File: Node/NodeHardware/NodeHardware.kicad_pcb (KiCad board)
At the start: 4 copper layers, 80 x 106 mm, 241 parts, among them J1 CONN_I2C, J10 DIG_IO_03, J11 ANA_IN_02, J12 PWR_OUT, J13 DIG_IO_02, J14 DIG_IO_04, J15 ANA_IN_03, J16 DIG_OUT_02, J17 ANA_IN_04, J2 USB_C_Receptacle_16P, J3 CONN_SPI, J4 PWR_IN, J5 ESP32_JTAG, J6 BATT, J7 ANA_IN_01, J8 DIG_OUT_01, J9 DIG_IO_01, Q1 AO3401A, Q2 AO3401A, Q3 2N7002, Q4 2N7002, Q5 AO3400A, Q6 AO3400A, SW1 RST, SW2 BOOT, SW3 BTN, U1 TPS565201DDCR, U2 CH340C, U3 SIM7000G_DEVBoard, U4 SPX3819M5-L-3-3, U5 MCP73831-2-OT, U6 ESP32-S3-WROOM-1, U7 ADS1220xPW, U8 ADS1220xPW

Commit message: Finish v1 of PCB layout
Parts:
- removed the C33 at (226.3, 111.4)
- removed the C33 at (243.3, 93.5)
- removed C37: 100n, Capacitor_SMD:C_0805_2012Metric
- removed the D15 at (263.9, 98.1)
- removed the D16 at (263.9, 102.3)
- removed the D23 at (256.8, 75.1)
- removed D27: BAT54S, Package_TO_SOT_SMD:SOT-23
- removed the R65 at (201.8, 93.4)
- removed the R65 at (206.2, 111.1)
- removed the R69 at (261.9, 71.6)
- removed the R69 at (206.2, 105.2)
- removed the R77 at (206.2, 114.0)
- removed the TP10 at (297.2, 141.0)
- removed the TP21 at (214.3, 78.5)
- removed the TP30 at (214.3, 72.4)
- removed the TP31 at (211.3, 75.5)
- removed TP37, TP53: TP_DIG_IO_06, TestPoint:TestPoint_Pad_D1.0mm
- removed TP38: TP_SPI_MISO, TestPoint:TestPoint_Pad_D1.0mm
- removed TP39: TP_SPI_CS_EXT, TestPoint:TestPoint_Pad_D1.0mm
- removed TP40: TP_DIG_OUT_01, TestPoint:TestPoint_Pad_D1.0mm
- removed TP41: TP_DIG_OUT_02, TestPoint:TestPoint_Pad_D1.0mm
- removed TP42: TP_ANA_IN_01, TestPoint:TestPoint_Pad_D1.0mm
- removed TP43: TP_ANA_IN_02, TestPoint:TestPoint_Pad_D1.0mm
- removed TP44: TP_ANA_IN_01_UC, TestPoint:TestPoint_Pad_D1.0mm
- removed TP45: TP_ANA_IN_02_UC, TestPoint:TestPoint_Pad_D1.0mm
- removed TP46: TP_ANA_IN_04, TestPoint:TestPoint_Pad_D1.0mm
- removed TP47: TP_ANA_IN_03, TestPoint:TestPoint_Pad_D1.0mm
- removed TP48: TP_DIG_IO_01, TestPoint:TestPoint_Pad_D1.0mm
- removed TP49: TP_DIG_IO_03, TestPoint:TestPoint_Pad_D1.0mm
- removed TP49: TP_DIG_IO_02, TestPoint:TestPoint_Pad_D1.0mm
- removed TP50: TP_ANA_IN_04_UC, TestPoint:TestPoint_Pad_D1.0mm
- removed TP51: TP_ANA_IN_03_UC, TestPoint:TestPoint_Pad_D1.0mm
- removed TP52: TP_DIG_IO_04, TestPoint:TestPoint_Pad_D1.0mm
- removed TP53: TP_DIG_IO_05, TestPoint:TestPoint_Pad_D1.0mm
- removed the TP6 at (248.6, 148.0)
- added C33: 100n, Capacitor_SMD:C_0805_2012Metric, F.Cu at (172.4, 124.4)
- added D21: BLUE, LED_SMD:LED_1210_3225Metric, F.Cu at (170.4, 105.2)
- added D24: BAT54S, Package_TO_SOT_SMD:SOT-23, F.Cu at (170.5, 71.1)
- added D26: BLUE, LED_SMD:LED_1210_3225Metric, F.Cu at (170.4, 74.7)
- added H1: GSM_MountingHole, MountingHole:MountingHole_3.2mm_M3_Pad_Via, F.Cu at (164.2, 100.6)
- added R65: 10k, Resistor_SMD:R_0805_2012Metric, F.Cu at (174.1, 101.5)
- added R69: 10k, Resistor_SMD:R_0805_2012Metric, F.Cu at (174.1, 105.2)
- added R73: 47R, Resistor_SMD:R_0805_2012Metric, F.Cu at (158.0, 113.4)
- added R78: 10k, Resistor_SMD:R_0805_2012Metric, F.Cu at (169.8, 68.0)
- added R79: 10k, Resistor_SMD:R_0805_2012Metric, F.Cu at (174.1, 84.7)
- added TP13: TP_I2C_SCL, TestPoint:TestPoint_Pad_D1.0mm, F.Cu at (123.4, 66.7)
- added TP24: TP_DIG_IO_02, TestPoint:TestPoint_Pad_D1.0mm, F.Cu at (167.4, 91.1)
- added TP33: TP_ANA_IN_01_UC, TestPoint:TestPoint_Pad_D1.0mm, F.Cu at (162.7, 118.2)
- added TP35: TP_ANA_IN_04_UC, TestPoint:TestPoint_Pad_D1.0mm, F.Cu at (162.7, 120.5)
- added TP9: TP_UART0_TX, TestPoint:TestPoint_Pad_D1.0mm, F.Cu at (160.8, 57.5)
- D17: value YELLOW -> BAT54S; footprint LED_SMD:LED_1210_3225Metric -> Package_TO_SOT_SMD:SOT-23
- D20: value BAT54S -> 3V6; footprint Package_TO_SOT_SMD:SOT-23 -> Diode_SMD:D_SOD-123
- D22, D25: value BAT54S -> BLUE; footprint Package_TO_SOT_SMD:SOT-23 -> LED_SMD:LED_1210_3225Metric
- R23: value 47k -> 2k
- R70: value 47R -> 10k
- R74: value 100R -> 47R
- R76: value 10k -> 100R
- TP11: value 3V3_Bypass_TP -> TP_SPI_CS_0; footprint TestPoint:TestPoint_Pad_D2.0mm -> TestPoint:TestPoint_Pad_D1.0mm
- TP12: value TP_UART0_TX -> TP_SPI_CS_1
- TP14: value TP_SPI_CS_0 -> TP_I2C_SDA
- TP15: value TP_SPI_CS_1 -> TP_DIGOUT_01
- TP16: value TP_I2C_SCL -> TP_DIGOUT_02
- TP17: value TP_I2C_SDA -> TP_GPIO6
- TP18: value TP_DIGOUT_01 -> TP_GPIO7
- TP19: value TP_DIGOUT_02 -> TP_GPIO8
- TP20: value TP_GPIO6 -> TP_GPIO9
- TP22: value TP_GPIO8 -> TP_GPIO11
- TP23: value TP_GPIO9 -> TP_DIG_IO_01
- TP25: value TP_GPIO11 -> TP_DIG_IO_03
- TP26: value TP_DIG_IO_01 -> TP_UART1_TX
- TP27: value TP_DIG_IO_02 -> TP_UART1_RX
- TP28: value TP_DIG_IO_03 -> TP_DIG_IO_04
- TP29: value TP_UART1_TX -> TP_DIG_IO_05
- TP32: value TP_DIG_IO_05 -> TP_DIG_IO_06
- TP34: value TP_SPI_MOSI -> TP_ANA_IN_02_UC
- TP36: value TP_SPI_SCLK -> TP_ANA_IN_03_UC
- moved D3 166.9 mm to (128.2, 132.2), turned to 180 degrees
- moved Q2 165.2 mm to (126.7, 136.2), turned to 180 degrees
- moved TP11 164.8 mm to (134.2, 107.2)
- moved C15 163.0 mm to (137.2, 133.8), turned to 90 degrees
- moved TH1 161.4 mm to (127.1, 119.6), turned to 180 degrees
- moved C12 161.3 mm to (137.9, 130.6), turned to 180 degrees
- moved U7 157.9 mm to (135.8, 116.0), turned to -90 degrees
- moved R45 153.6 mm to (130.7, 119.6), turned to 180 degrees
- moved C22 152.4 mm to (134.1, 121.9), turned to 90 degrees
- moved C26 152.1 mm to (127.1, 117.5), turned to 180 degrees
- moved R53 151.6 mm to (136.2, 121.9), turned to 90 degrees
- moved R52 150.9 mm to (138.3, 121.9), turned to 90 degrees
- moved C23 150.4 mm to (130.7, 117.5), turned to 0 degrees
- moved C13 150.1 mm to (159.7, 134.4), turned to 180 degrees
- moved R46 149.0 mm to (127.1, 115.4), turned to 180 degrees
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- renumbered D18 to D15, D19 to D16, D21 to D18, D22 to D19, D24 to D23, H1 to H2, H2 to H3, H3 to H4, H4 to H5, R73 to R75, R75 to R77, TP13 to TP10, TP24 to TP21, TP33 to TP30, TP35 to TP31, TP7 to TP6, TP8 to TP7, TP9 to TP8
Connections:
- C14 pad 1: +BATT -> /3V3_LP_REG_IN
- D17 pad 2: /MCU_And_Peripherals/SPI_CS_LED_0_K -> +3V3
- D20 pad 1: GND -> ANA_IN_03_UC
- D20 pad 2: +3V3 -> GND
- D22 pad 2: +3V3 -> Net-(D22-A)
- D25 pad 2: +3V3 -> Net-(D25-A)
- R70 pad 1: Net-(U8-DIN) -> DIG_IO_02
- R70 pad 2: SPI_MOSI -> Net-(D22-A)
- R71 pad 1: Net-(U8-DOUT/~{DRDY}) -> Net-(U8-SCLK)
- R71 pad 2: SPI_MISO -> SPI_SCLK
- R72 pad 1: Net-(U8-~{CS}) -> Net-(U8-DIN)
- R72 pad 2: SPI_CS_ADC1 -> SPI_MOSI
- R74 pad 1: DIG_IO_04_UC -> Net-(U8-~{CS})
- R74 pad 2: DIG_IO_04 -> SPI_CS_ADC1
- R76 pad 2: GND -> DIG_IO_04
- R80 pad 1: DIG_IO_06_UC -> DIG_IO_04
- R80 pad 2: GND -> Net-(D26-A)
- TP11 pad 1: Net-(U4-BP) -> SPI_CS_ADC0
- TP12 pad 1: UART0_UC_TX -> SPI_CS_ADC1
- TP14 pad 1: SPI_CS_ADC0 -> I2C_SDA
- TP15 pad 1: SPI_CS_ADC1 -> DIG_OUT_01_UC
- TP16 pad 1: I2C_SCL -> DIG_OUT_02_UC
- TP17 pad 1: I2C_SDA -> Net-(U6-GPIO6/TOUCH6/ADC1_CH5)
- TP18 pad 1: DIG_OUT_01_UC -> Net-(U6-GPIO7/TOUCH7/ADC1_CH6)
- TP19 pad 1: DIG_OUT_02_UC -> Net-(U6-GPIO8/TOUCH8/ADC1_CH7/SUBSPICS1)
- TP20 pad 1: Net-(U6-GPIO6/TOUCH6/ADC1_CH5) -> Net-(U6-GPIO9/TOUCH9/ADC1_CH8/FSPIHD/SUBSPIHD)
- TP22 pad 1: Net-(U6-GPIO8/TOUCH8/ADC1_CH7/SUBSPICS1) -> Net-(U6-GPIO11/TOUCH11/ADC2_CH0/FSPID/FSPIIO5/SUBSPID)
- TP23 pad 1: Net-(U6-GPIO9/TOUCH9/ADC1_CH8/FSPIHD/SUBSPIHD) -> DIG_IO_01_UC
- TP25 pad 1: Net-(U6-GPIO11/TOUCH11/ADC2_CH0/FSPID/FSPIIO5/SUBSPID) -> DIG_IO_03_UC
- TP26 pad 1: DIG_IO_01_UC -> UART1_UC_TX
- TP27 pad 1: DIG_IO_02_UC -> UART1_UC_RX
- TP28 pad 1: DIG_IO_03_UC -> DIG_IO_04_UC
- TP29 pad 1: UART1_UC_TX -> LED_01
- TP32 pad 1: LED_01 -> LED_02
- TP34 pad 1: SPI_MOSI -> ANA_IN_02_UC
- TP36 pad 1: SPI_SCLK -> ANA_IN_03_UC
- U4 pad 4: Net-(U4-BP) -> unconnected-(U4-BP-Pad4)
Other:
- board text added: "- BATT +"
- board text added: "- PWR +"
- board text added: "3V3"
- board text added: "3V3 RST TCK TDO TDI TMS GND"
- board text added: "5V"
- board text added: "ANA_IN_01 - +"
- board text added: "ANA_IN_02 - +"
- board text added: "ANA_IN_03 - +"
- board text added: "ANA_IN_04 - +"
- board text added: "BATT"
- board text added: "BOOT"
- board text added: "BTN"
- board text added: "CS"
- board text added: "DIG_IO_01 - +"
- board text added: "DIG_IO_02 - +"
- board text added: "DIG_IO_03 - +"
- board text added: "DIG_IO_04 - +"
- board text added: "DIG_OUT_01 - +"
- board text added: "DIG_OUT_02 - +"
- board text added: "ESP32 S3 WROOM-1"
- board text added: "ESP32 based IoT breakout board"
- board text added: "GND"
- board text added: "GSM Module"
- board text added: "I2C"
- board text added: "INPUT ADC"
- board text added: "JTAG"
- board text added: "MISO"
- board text added: "MOSI"
- board text added: "RST"
- board text added: "SCL"
- board text added: "SCLK"
- board text added: "SDA"
- board text added: "SENSOR ADC"
- board text added: "SPI"
- board text added: "STATUS"
- board text added: "SUPPLY OUT"
- board text added: "UC_RX"
- board text added: "UC_TX"
- board text added: "V1.0"
- board text added: "V_IN"
- board text added: "WiFi"
- board text added: "github.com/AleksaHeler/FlexNode"

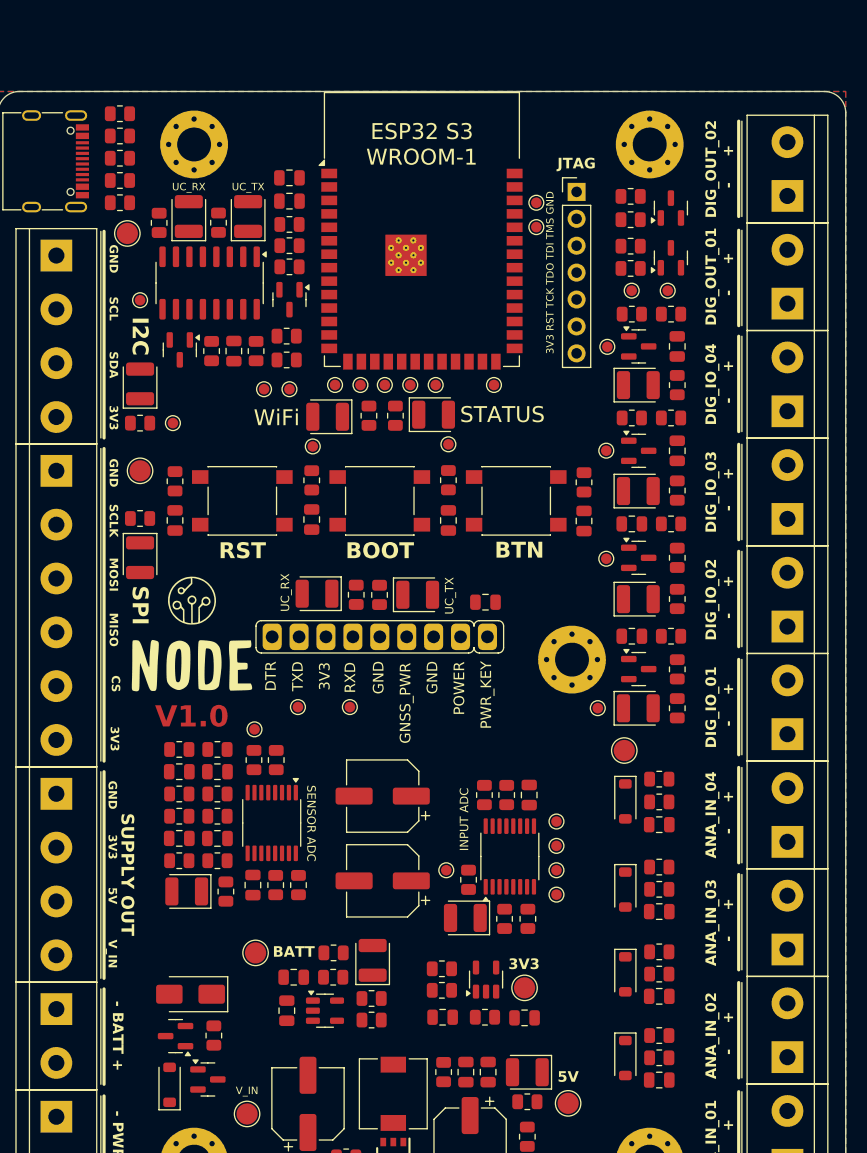
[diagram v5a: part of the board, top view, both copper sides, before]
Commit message: Update SW side of the Node
Still a lot of cleanup and work remains
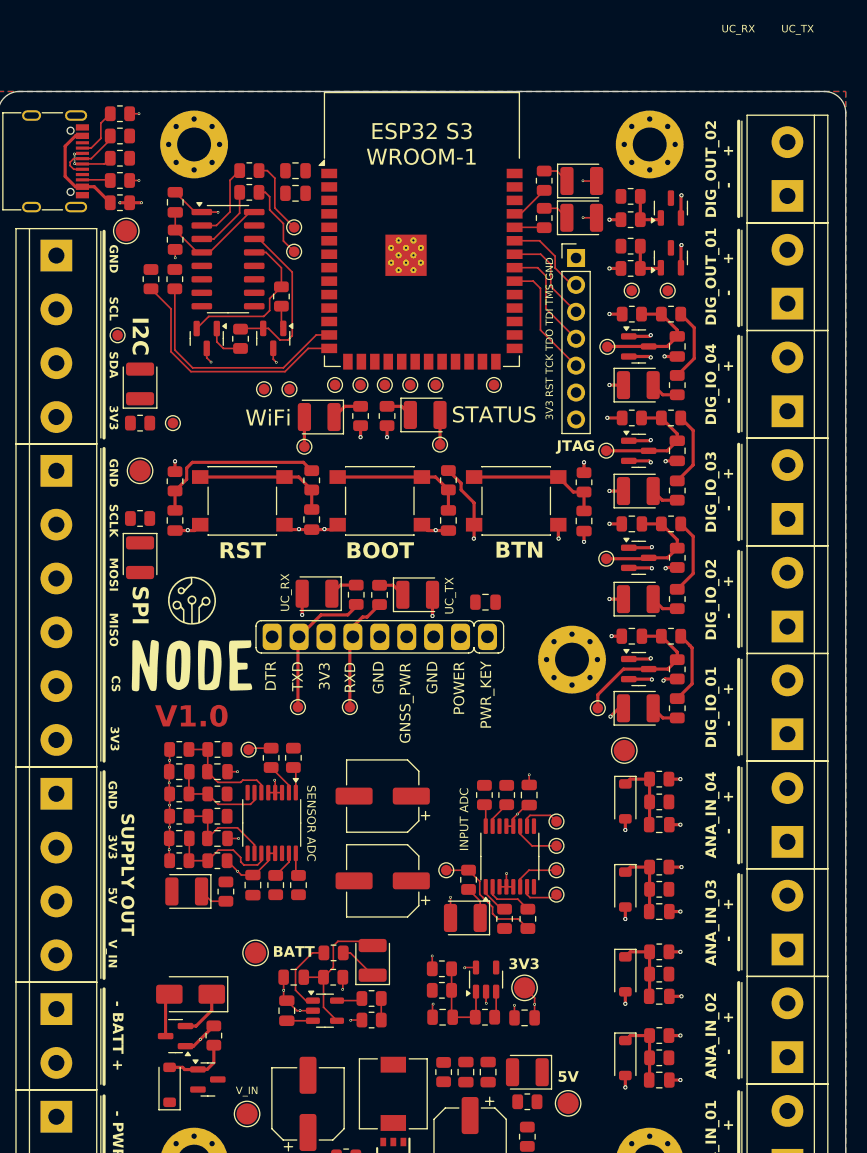
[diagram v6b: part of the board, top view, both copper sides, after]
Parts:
- moved D8 37.1 mm to (165.1, 58.9), turned to 0 degrees
- moved R24 36.3 mm to (161.5, 58.9), turned to -90 degrees
- moved D9 31.7 mm to (165.1, 55.5), turned to 0 degrees
- moved R25 31.0 mm to (161.5, 55.4), turned to -90 degrees
- moved TP9 23.3 mm to (137.9, 62.1), turned to 180 degrees
- moved TP10 22.9 mm to (137.9, 59.8), turned to 180 degrees
- moved C8 15.1 mm to (126.7, 57.5), turned to 90 degrees
- moved R32 14.9 mm to (124.4, 64.7), turned to -90 degrees
- moved R10 13.0 mm to (126.7, 61.0)
- moved R34 11.8 mm to (126.7, 64.7), turned to -90 degrees
- moved R13 8.03 mm to (133.7, 54.5)
- moved J5 6.24 mm to (164.6, 62.7)
- moved R14 4.85 mm to (133.7, 56.5)
- moved Q3 3.96 mm to (136.0, 70.3)
- moved TP13 3.93 mm to (121.3, 70.0)
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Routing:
- net GND: track 0.00 -> 96.9 mm, vias 0 -> 60
- net +3V3: track 0.00 -> 41.8 mm, vias 0 -> 17
- net Net-(U6-GPIO20/U1CTS/ADC2_CH9/CLK_OUT1/USB_D+): track 0.00 -> 23.3 mm
- net Net-(U6-GPIO19/U1RTS/ADC2_CH8/CLK_OUT2/USB_D-): track 0.00 -> 22.3 mm
- net RST: track 0.00 -> 18.2 mm, vias 0 -> 1
- net CH340_RTS: track 0.00 -> 16.4 mm
- net CH340_DTR: track 0.00 -> 15.3 mm
- net DIG_IO_01_UC: track 0.00 -> 14.8 mm
- net BOOT: track 0.00 -> 14.4 mm, vias 0 -> 1
- net Net-(D4-A): track 0.00 -> 13.9 mm
- net UART1_UC_RX: track 0.00 -> 13.4 mm
- net Net-(C19-Pad1): track 0.00 -> 12.9 mm
- net USER_BUTTON: track 0.00 -> 12.7 mm
- net DIG_IO_02_UC: track 0.00 -> 11.9 mm
- net DIG_IO_03_UC: track 0.00 -> 11.7 mm
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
